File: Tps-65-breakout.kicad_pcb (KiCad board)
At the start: 2 copper layers, 19.9 x 18.5 mm, 6 parts, among them J1 Conn_01x06_Pin, J2 Conn_01x06_Socket

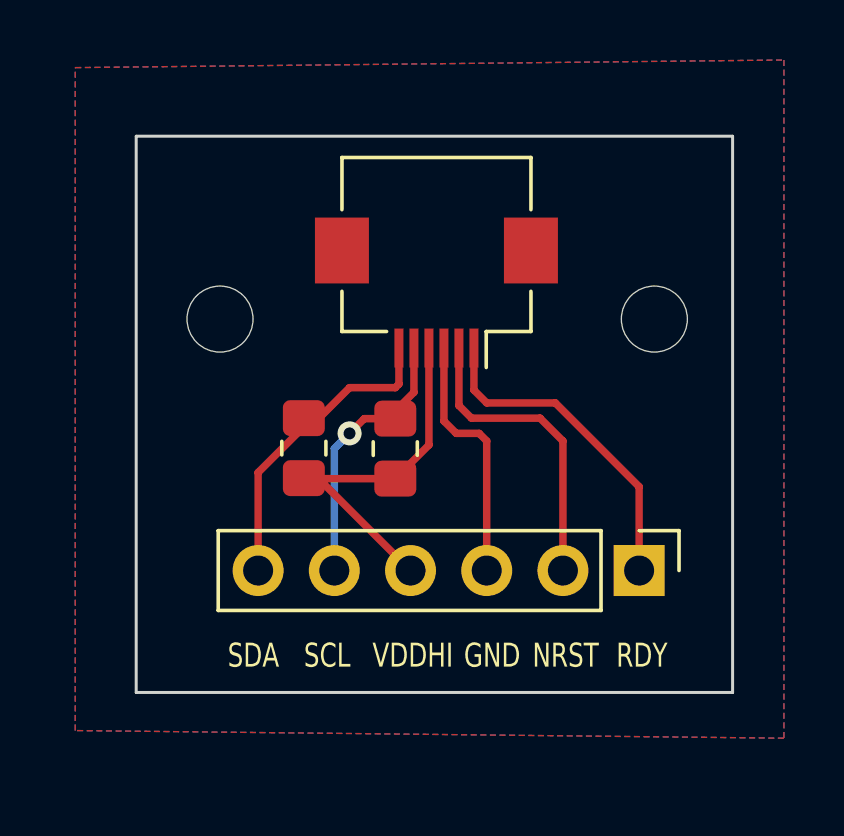
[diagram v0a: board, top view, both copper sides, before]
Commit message: improved routing and grounded mounting holes
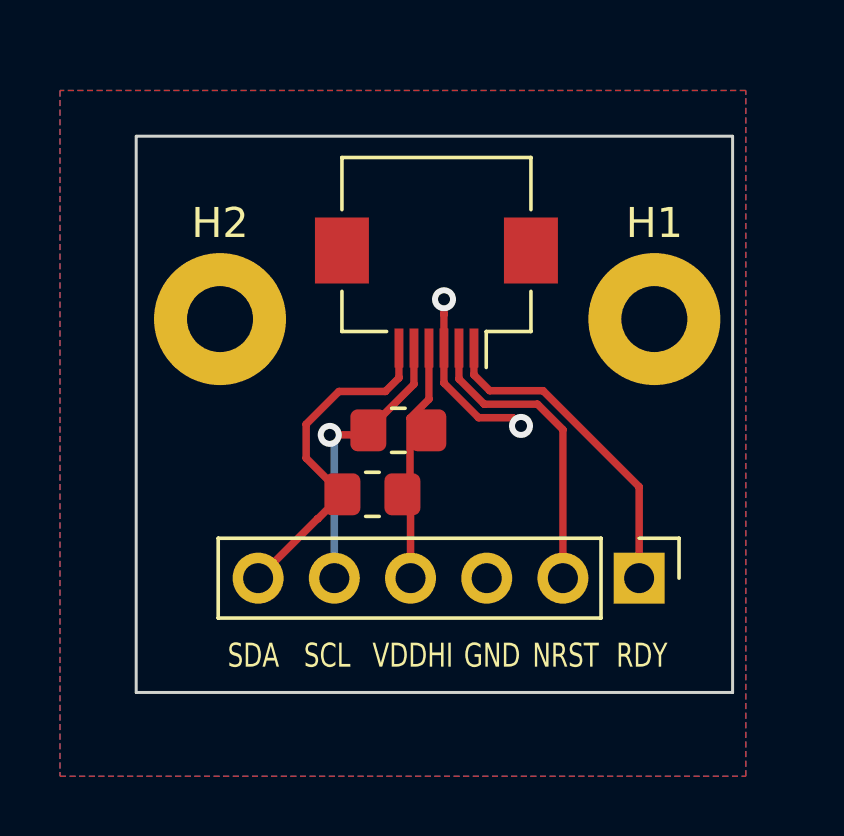
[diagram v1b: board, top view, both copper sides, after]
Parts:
- H1, H2: footprint MountingHole:MountingHole_2.2mm_M2 -> MountingHole:MountingHole_2.2mm_M2_Pad
- moved R2 2.76 mm to (129.8, 69.3), turned to 180 degrees
- moved R1 0.62 mm to (130.7, 67.2), turned to 180 degrees
- moved J2 0.25 mm to (138.7, 72.1)
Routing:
- net VDDHI: track 11.7 -> 7.90 mm
- net GND: track 8.46 -> 5.97 mm, vias 0 -> 2
- net SDA: track 10.4 -> 11.5 mm

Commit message: reversed pin order, grounded ffc connector, added silkscreens
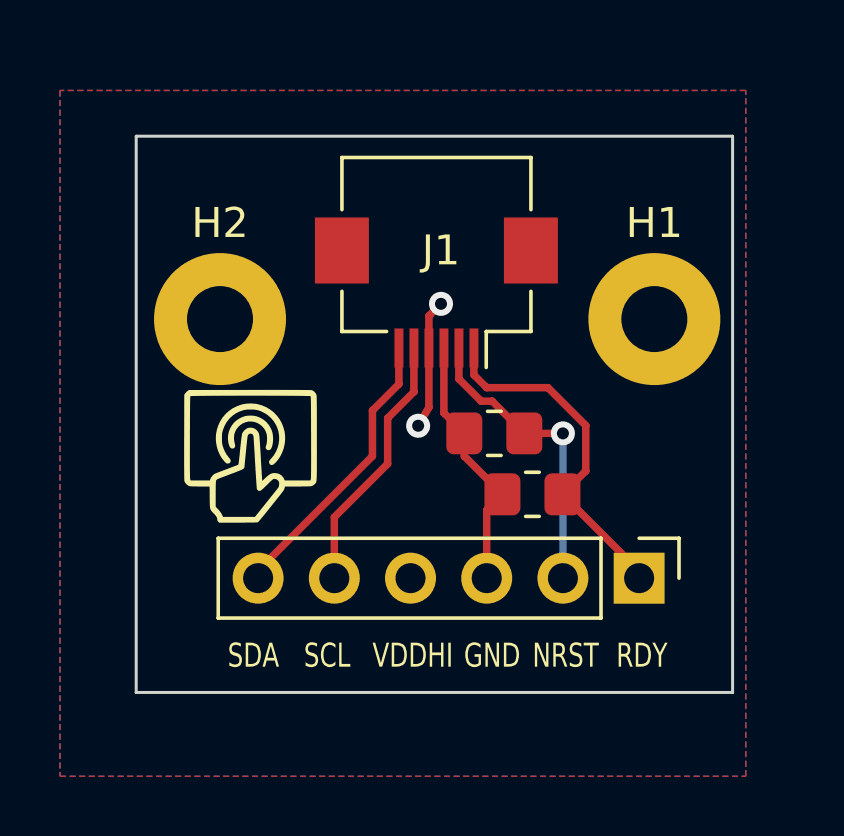
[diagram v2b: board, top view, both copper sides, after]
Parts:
- added G***: LOGO, project:trackpad_symbol, F.Cu at (125.7, 68.1)
- moved R2 5.33 mm to (135.1, 69.3)
- moved R1 3.20 mm to (133.9, 67.3)
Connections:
- J1 pad 1: RDY -> SDA
- J1 pad 2: NRST -> SCL
- J1 pad 3: GND -> VDDHI
- J1 pad 4: VDDHI -> GND
- J1 pad 5: SCL -> NRST
- J1 pad 6: SDA -> RDY
- J1 pad MP: (no net) -> GND
- J2 pad 1: RDY -> SDA
- J2 pad 2: NRST -> SCL
- J2 pad 3: GND -> VDDHI
- J2 pad 4: VDDHI -> GND
- J2 pad 5: SCL -> NRST
- J2 pad 6: SDA -> RDY
- R1 pad 1: VDDHI -> SCL
- R1 pad 2: SCL -> VDDHI
- R2 pad 1: VDDHI -> SDA
- R2 pad 2: SDA -> VDDHI
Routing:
- net GND: track 5.97 -> 4.58 mm
- net NRST: track 9.90 -> 8.77 mm
- net RDY: track 10.7 -> 9.62 mm
- net VDDHI: track 7.90 -> 8.70 mm
- net SCL: track 9.30 -> 10.1 mm
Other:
- board text added: "Tps-65/43 breakout board Rev 1.0"
- board text added: "https://github.com/KweBoakye/Tps-65-breakout"
